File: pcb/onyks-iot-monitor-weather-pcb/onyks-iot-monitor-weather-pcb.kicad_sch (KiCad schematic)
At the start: 17 parts, among them SW1 BOOT, SW2 ENABLE, U1 ESP32-WROOM-32D, U2 SHT30-DIS

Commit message: Added schematic for our project
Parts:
- removed C6: C, symbol Device:C
- removed R2, R3: 10k, symbol Device:R
- removed U2: SHT30-DIS, Sensor_Humidity:Sensirion_DFN-8-1EP_2.5x2.5mm_P0.5mm_EP1.1x1.7mm, symbol Sensor_Humidity:SHT30-DIS
- added U10, U11, U12, U13, U8, U9: DRV5033AJxLPG, Package_TO_SOT_THT:TO-92_Inline, symbol Sensor_Magnetic:DRV5033AJxLPG
- added U2, U7: AMS1117, Package_TO_SOT_SMD:SOT-223-3_TabPin2, symbol Regulator_Linear:AMS1117
- added U3: AM2302, Sensor:ASAIR_AM2302_P2.54mm_Vertical, symbol Sensor:AM2302
- added U4: ~, symbol 1BMoje:PMS5003
- added U5: ~, symbol 1BMoje:SEN0219
- added U6: BMP280, Package_LGA:Bosch_LGA-8_2x2.5mm_P0.65mm_ClockwisePinNumbering, symbol Sensor_Pressure:BMP280
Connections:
- net GND: now also U1.1 (GND), U1.15 (GND), U1.38 (GND), U1.39 (GND), U10.2 (GND), U11.2 (GND), U12.2 (GND), U13.2 (GND), U2.1 (ADJ), U3.3 (GND), U3.4 (GND), U4.2 (GND), U5.3 (GND), U6.1 (GND), U6.7 (GND), U7.1 (ADJ), U8.2 (GND), U9.2 (GND)
- net VCC: now also U10.1 (VCC), U11.1 (VCC), U12.1 (VCC), U13.1 (VCC), U2.3 (VI), U3.1 (VDD), U4.1 (VCC), U5.2 (VCC), U7.3 (VI), U8.1 (VCC), U9.1 (VCC); no longer U1.2 (VDD)
- net Hall 1: now reaches U1.10 (IO25)
- net Hall 1: now also U9.3 (OUT)
- net Hall 2: now reaches U1.11 (IO26)
- net Hall 2: now also U8.3 (OUT)
- net Hall 3: now reaches U1.12 (IO27)
- net Hall 3: now also U10.3 (OUT)
- net Hall 6: now reaches U1.13 (IO14)
- net Hall 6: now also U12.3 (OUT)
- net BMP_SCK: now reaches U1.20 (SCK/CLK)
- net BMP_SCK: now also U6.4 (SCK)
- net BMP_SDO: now reaches U1.21 (SDO/SD0)
- net BMP_SDO: now also U6.5 (SDO)
- net BMP_SDI: now reaches U1.22 (SDI/SD1)
- net BMP_SDI: now also U6.3 (SDI)
- net PMS_SELECT: now reaches U1.23 (IO15)
- net PMS_SELECT: now also U4.8 (ModeSelect)
- net PMS_SET: now reaches U1.24 (IO2)
- net PMS_SET: now also U4.3 (SET)
- net PMS_RXD: now reaches U1.34 (RXD0/IO3)
- net PMS_RXD: now also U4.4 (RXD)
- net PMS_TXD: now reaches U1.35 (TXD0/IO1)
- net PMS_TXD: now also U4.5 (TXD)
- net PMS_RESET: now reaches U1.36 (IO22)
- net PMS_RESET: now also U4.6 (RESET)
- net Hall 5: now reaches U1.6 (IO34)
- net Hall 5: now also U13.3 (OUT)
- net PMS_PWM: now reaches U1.7 (IO35)
- net PMS_PWM: now also U4.7 (PWM)
- net Hall 4: now reaches U1.8 (IO32)
- net Hall 4: now also U11.3 (OUT)
- net SCL renamed SEN0219
- net SEN0219: now also U5.1 (Signal)
- net SDA renamed DHT22
- net DHT22: now also U3.2 (SDA)
- new net: U1.2 (VDD), U2.2 (VO)
- new net BMP_CSB: U6.2 (CSB), U6.6 (VDDIO), U6.8 (VDD), U7.2 (VO)
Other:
- note added: "BMP280 - pressure sensor"
- note added: "DHT22 - Temperature and humidity sensor"
- note added: "Hall effect sensors - quantity of rain"
- note added: "Hall effect sensors - wind direction"
- note added: "Hall effect sensors - wind speed"
- note added: "INFRARED CO2 sensor SEN0219"
- note added: "PMS5003 - Air quality sensor"
- note removed: "Temperature and Humidity Sensor"
- moved on the sheet: C1, C2, C3, C4, C5, D1, R1, R4, R5, R6, SW1, SW2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

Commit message: Updated schematics and added footprints and 3dmodels for the elements
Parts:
- removed D1: LED_KRGB, symbol Device:LED_KRGB
- removed R4, R5, R6: 300, symbol Device:R
- removed SW1: BOOT, symbol Switch:SW_Push
- removed SW2: ENABLE, symbol Switch:SW_Push
- removed U10, U11, U12, U13, U8, U9: DRV5033AJxLPG, Package_TO_SOT_THT:TO-92_Inline, symbol Sensor_Magnetic:DRV5033AJxLPG
- removed U3: AM2302, Sensor:ASAIR_AM2302_P2.54mm_Vertical, symbol Sensor:AM2302
- removed U4: ~, symbol 1BMoje:PMS5003
- removed U5: ~, symbol 1BMoje:SEN0219
- removed U7: AMS1117, Package_TO_SOT_SMD:SOT-223-3_TabPin2, symbol Regulator_Linear:AMS1117
- added J1, J2, J4, J5, J6, J7, J8, J9: 53398-0371, 1bmoje:53398-0371, symbol 1BMoje:53398-0371
- added J10: Conn_01x02_Pin, Connector_Molex:Molex_SL_171971-0002_1x02_P2.54mm_Vertical, symbol Connector:Conn_01x02_Pin
- added J3: 53048-0810, 530480810, symbol 1BMoje:53048-0810
- added Q1, Q2: SS8050, Package_TO_SOT_SMD:SOT-23, symbol Transistor_BJT:SS8050
- added R2, R3: 10K, Resistor_SMD:R_0201_0603Metric, symbol Device:R
- added S1: BOOT, 18259106, symbol 1BMoje:1825910-6
- added S2: ENABLE, 18259106, symbol 1BMoje:1825910-6
- C1: value 22 uF -> 22uF; footprint (none) -> Capacitor_SMD:C_0201_0603Metric
- C2: footprint (none) -> Capacitor_SMD:C_0201_0603Metric
- C3: value C -> 0.1uF; footprint (none) -> Capacitor_SMD:C_0201_0603Metric
- C4, C5: value 0.1 uF -> 0.1uF; footprint (none) -> Capacitor_SMD:C_0201_0603Metric
- R1: value R -> 10K; footprint (none) -> Resistor_SMD:R_0201_0603Metric
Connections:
- net BMP_CSB is gone; now on net 3V3: U6.2 (CSB), U6.6 (VDDIO), U6.8 (VDD)
- net DHT22: now also J9.2
- net EN: now also Q1.3 (C), S2.2 (COM_2), S2.4 (NO_2)
- net GND: now also J1.2, J2.2, J3.2, J4.2, J5.2, J6.2, J7.2, J8.3, J9.3, S1.1 (COM_1), S1.3 (NO_1), S2.1 (COM_1), S2.3 (NO_1)
- net Hall 1: now also J4.3
- net Hall 2: now also J5.3
- net Hall 3: now also J6.3
- net Hall 4: now also J7.3
- net Hall 5: now also J2.3
- net Hall 6: now also J1.3
- net IO0: now also Q2.2 (E), S1.2 (COM_2), S1.4 (NO_2)
- net PMS_PWM: now also J3.7
- net PMS_RESET: now also J3.6
- net PMS_RXD: now also J3.4
- net PMS_SELECT: now also J3.8
- net PMS_SET: now also J3.3
- net PMS_TXD: now also J3.5
- net SEN0219: now also J8.1
- net VCC: now also J1.1, J2.1, J3.1, J4.1, J5.1, J6.1, J7.1, J8.2, J9.1
- net 3V3: now reaches U1.2 (VDD), U2.2 (VO)
- new net: J10.1 (Pin_1), Q2.3 (C), R2.1
- new net: Q1.1 (B), R2.2
- new net: J10.2 (Pin_2), Q1.2 (E), R3.1
- new net: Q2.1 (B), R3.2
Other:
- note added: "For programming"

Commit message: Added PCBv1.0
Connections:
- net 3V3: now also C1.1, C2.1, R1.1
- net IO0: now also U1.25 (IO0)
- net VCC: no longer C1.1, C2.1, R1.1
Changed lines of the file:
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@@
 	(wire
 		(pts
+			(xy 260.35 45.72) (xy 265.43 45.72)
+		)
+		(stroke
+			(width 0)
+			(type default)
+		)
+	)
+	(wire
+		(pts
 			(xy 245.11 27.94) (xy 245.11 40.64)
 		)
@@
 		)
 	)
+	(label "IO0"
+		(at 265.43 45.72 0)
+		(fields_autoplaced yes)
+		(effects
+			(font
+				(size 1.27 1.27)
+			)
+			(justify left bottom)
+		)
+	)
 	(label "PMS_TXD"
 		(at 144.78 91.44 0)
@@
 		)
 	)
+	(label "3V3"
+		(at 187.96 35.56 0)
+		(fields_autoplaced yes)
+		(effects
+			(font
+				(size 1.27 1.27)
+			)
+			(justify left bottom)
+		)
+	)
 	(label "BMP_CSB"
 		(at 129.54 163.83 0)
@@
 		)
 	)
+	(label "3V3"
+		(at 187.96 82.55 0)
+		(fields_autoplaced yes)
+		(effects
+			(font
+				(size 1.27 1.27)
+			)
+			(justify left bottom)
+		)
+	)
 	(label "BMP_SDO"
 		(at 129.54 161.29 0)
@@
 	)
 	(symbol
-		(lib_id "power:VCC")
-		(at 187.96 82.55 0)
-		(unit 1)
-		(exclude_from_sim no)
-		(in_bom yes)
-		(on_board yes)
-		(dnp no)
-		(fields_autoplaced yes)
-		(property "Reference" "#PWR05"
-			(at 187.96 86.36 0)
-			(effects
-				(font
-					(size 1.27 1.27)
-				)
-				(hide yes)
-			)
-		)
-		(property "Value" "VCC"
-			(at 187.96 77.47 0)
-			(effects
-				(font
-					(size 1.27 1.27)
-				)
-			)
-		)
-		(property "Footprint" ""
-			(at 187.96 82.55 0)
-			(effects
-				(font
-					(size 1.27 1.27)
-				)
-				(hide yes)
-			)
-		)
-		(property "Datasheet" ""
-			(at 187.96 82.55 0)
-			(effects
-				(font
-					(size 1.27 1.27)
-				)
-				(hide yes)
-			)
-		)
-		(property "Description" "Power symbol creates a global label with name \"VCC\""
-			(at 187.96 82.55 0)
-			(effects
-				(font
-					(size 1.27 1.27)
-				)
-				(hide yes)
-			)
-		)
-		(pin "1"
-		)
-		(instances
-			(project "onyks-iot-monitor-weather-pcb"
-				(path "/c76e8e74-1f9a-4d6f-ac1c-451a63f003ec"
-					(reference "#PWR05")
-					(unit 1)
-				)
-			)
-		)
-	)
-	(symbol
 		(lib_id "Device:C")
 		(at 208.28 58.42 0)
@@
 					(unit 1)
 				)
-			)
-		)
-	)
-	(symbol
-		(lib_id "power:VCC")
-		(at 187.96 35.56 0)
-		(unit 1)
-		(exclude_from_sim no)
-		(in_bom yes)
-		(on_board yes)
-		(dnp no)
-		(fields_autoplaced yes)
-		(property "Reference" "#PWR03"
-			(at 187.96 39.37 0)
-			(effects
-				(font
-					(size 1.27 1.27)
-				)
-				(hide yes)
-			)
-		)
-		(property "Value" "VCC"
-			(at 187.96 30.48 0)
-			(effects
-				(font
-					(size 1.27 1.27)
-				)
-			)
-		)
-		(property "Footprint" ""
-			(at 187.96 35.56 0)
-			(effects
-				(font
-					(size 1.27 1.27)
-				)
-				(hide yes)
-			)
-		)
-		(property "Datasheet" ""
-			(at 187.96 35.56 0)
-			(effects
-				(font
-					(size 1.27 1.27)
-				)
-				(hide yes)
-			)
-		)
-		(property "Description" "Power symbol creates a global label with name \"VCC\""
-			(at 187.96 35.56 0)
-			(effects
-				(font
-					(size 1.27 1.27)
-				)
-				(hide yes)
-			)
-		)
-		(pin "1"
-		)
-		(instances
-			(project ""
-				(path "/c76e8e74-1f9a-4d6f-ac1c-451a63f003ec"
-					(reference "#PWR03")
-					(unit 1)
-				)

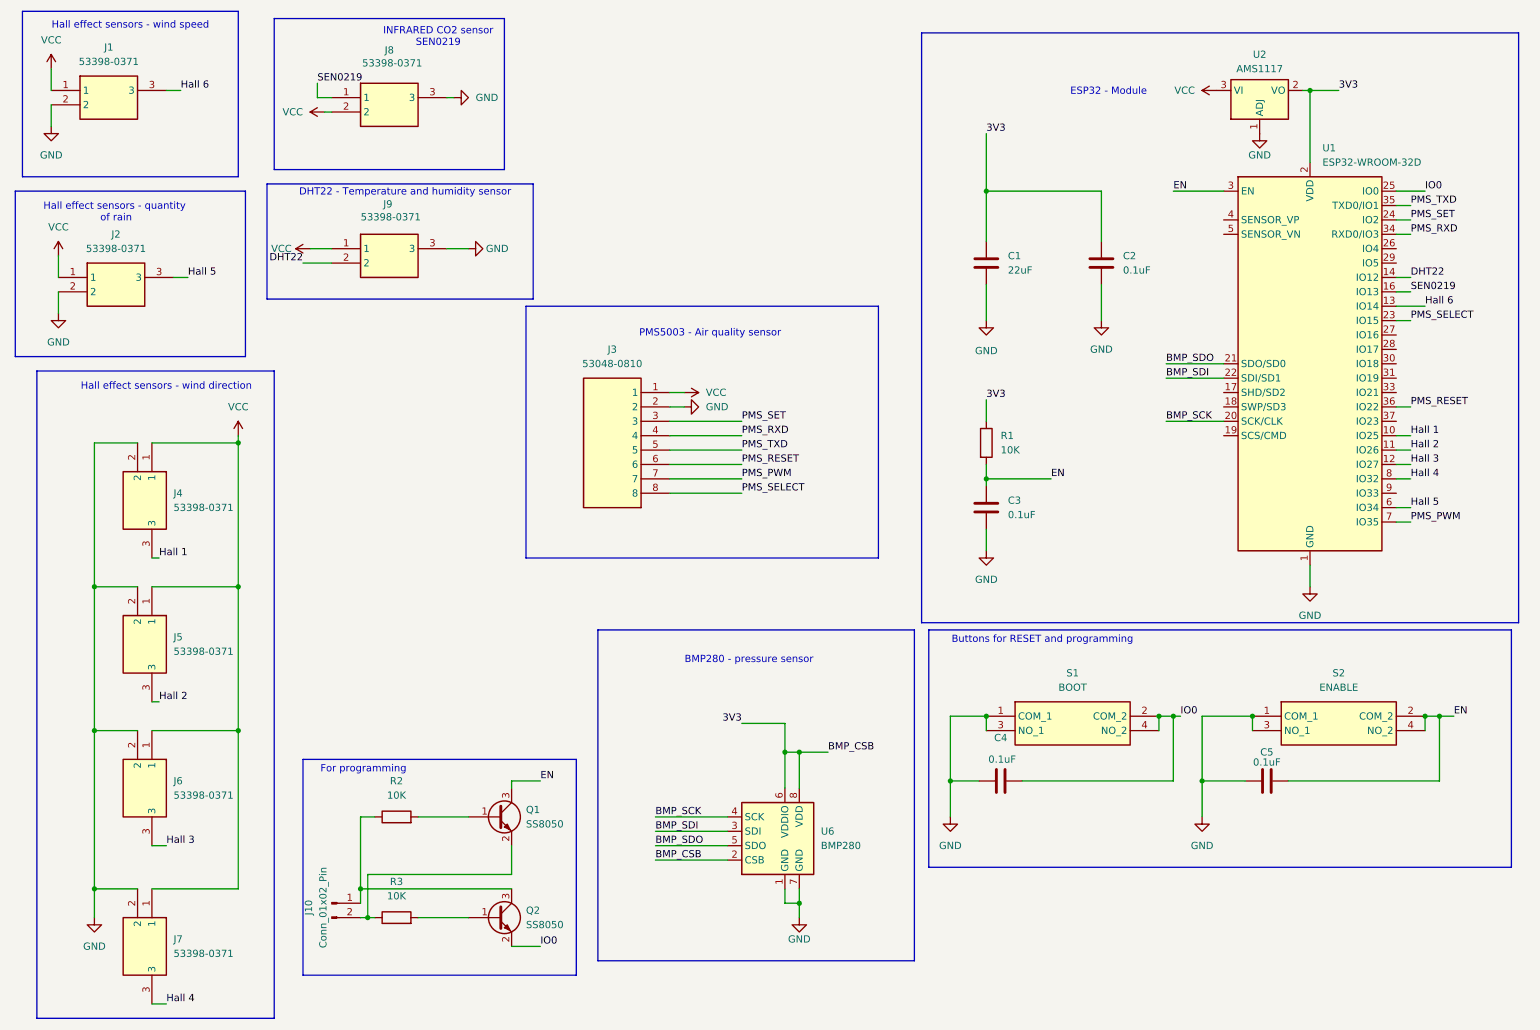
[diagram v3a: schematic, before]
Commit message: Updated schematic, changed and added couple of elements: 1.Changed buttons; 2.Changed Voltage Regulator; 3.Changed LED; 4.Added JTAG interface; 5.Added UART for programming; 6.Added other elements like capacitors etc.
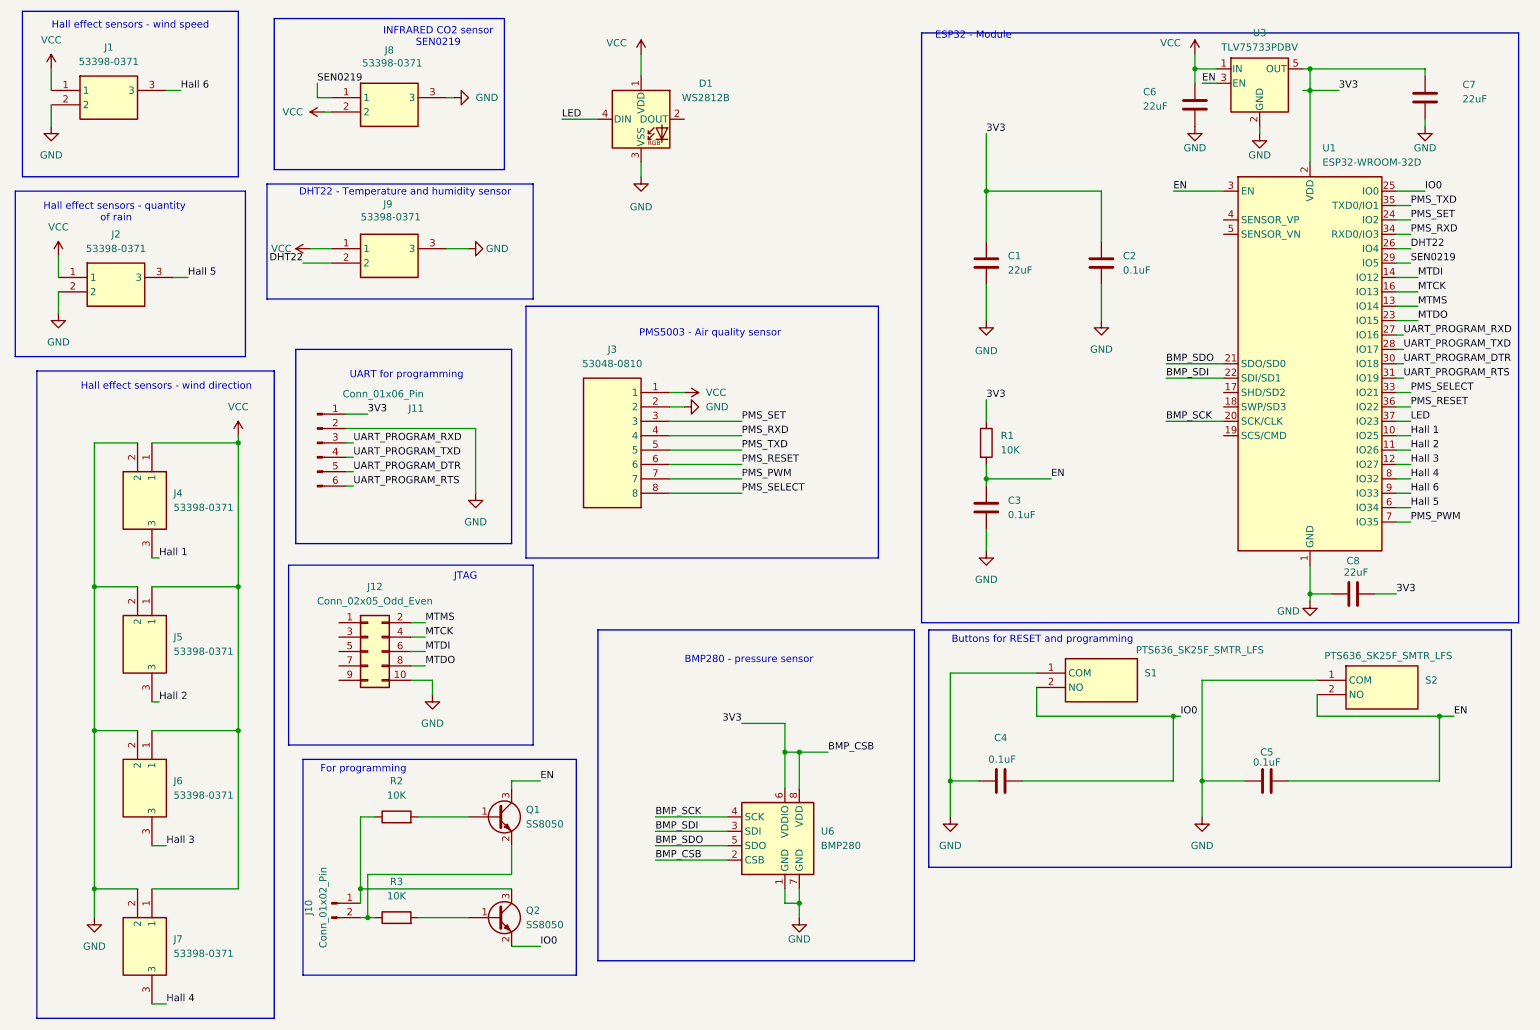
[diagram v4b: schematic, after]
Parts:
- removed S1: BOOT, 18259106, symbol 1BMoje:1825910-6
- removed S2: ENABLE, 18259106, symbol 1BMoje:1825910-6
- removed U2: AMS1117, Package_TO_SOT_SMD:SOT-223-3_TabPin2, symbol Regulator_Linear:AMS1117
- added C6, C7, C8: 22uF, Capacitor_SMD:C_0201_0603Metric, symbol Device:C
- added D1: WS2812B, LED_SMD:LED_WS2812B_PLCC4_5.0x5.0mm_P3.2mm, symbol LED:WS2812B
- added J11: Conn_01x06_Pin, Connector_PinHeader_2.54mm:PinHeader_1x06_P2.54mm_Vertical, symbol Connector:Conn_01x06_Pin
- added J12: Conn_02x05_Odd_Even, Connector_PinHeader_2.54mm:PinHeader_2x05_P2.54mm_Vertical, symbol Connector_Generic:Conn_02x05_Odd_Even
- added S1, S2: PTS636_SK25F_SMTR_LFS, 1bmoje:PTS636SK25FSMTRLFS, symbol 1BMoje:PTS636_SK25F_SMTR_LFS
- added U3: TLV75733PDBV, Package_TO_SOT_SMD:SOT-23-5, symbol Regulator_Linear:TLV75733PDBV
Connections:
- net 3V3: now also C7.1, C8.2, J11.1 (Pin_1), U3.5 (OUT)
- net DHT22: now also U1.26 (IO4); no longer U1.14 (IO12)
- net EN: now also S2.2 (NO), U3.3 (EN)
- net GND: now also C6.2, C7.2, C8.1, D1.3 (VSS), J11.2 (Pin_2), J12.10 (Pin_10), S1.1 (COM), S2.1 (COM), U3.2 (GND)
- net Hall 6: now also U1.9 (IO33); no longer U1.13 (IO14)
- net IO0: now also S1.2 (NO)
- net PMS_SELECT: now also U1.33 (IO21); no longer U1.23 (IO15)
- net SEN0219: now also U1.29 (IO5); no longer U1.16 (IO13)
- net VCC: now also C6.1, D1.1 (VDD), U3.1 (IN)
- net UART_PROGRAM_RXD: now reaches U1.27 (IO16)
- net UART_PROGRAM_RXD: now also J11.3 (Pin_3)
- net UART_PROGRAM_TXD: now reaches U1.28 (IO17)
- net UART_PROGRAM_TXD: now also J11.4 (Pin_4)
- net UART_PROGRAM_DTR: now reaches U1.30 (IO18)
- net UART_PROGRAM_DTR: now also J11.5 (Pin_5)
- net UART_PROGRAM_RTS: now reaches U1.31 (IO19)
- net UART_PROGRAM_RTS: now also J11.6 (Pin_6)
- net LED: now reaches U1.37 (IO23)
- net LED: now also D1.4 (DIN)
- new net MTCK: J12.4 (Pin_4), U1.16 (IO13)
- new net MTDI: J12.6 (Pin_6), U1.14 (IO12)
- new net MTDO: J12.8 (Pin_8), U1.23 (IO15)
- new net MTMS: J12.2 (Pin_2), U1.13 (IO14)
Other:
- note added: "JTAG"
- note added: "UART for programming"

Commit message: Done my version of PCB
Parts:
- added J13: Conn_01x02_Pin, Connector_PinHeader_2.54mm:PinHeader_1x02_P2.54mm_Vertical, symbol Connector:Conn_01x02_Pin
- J10: footprint Connector_Molex:Molex_SL_171971-0002_1x02_P2.54mm_Vertical -> Connector_PinHeader_2.54mm:PinHeader_1x02_P2.54mm_Vertical
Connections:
- net 3V3: now also J12.1 (Pin_1)
- net GND: now also J12.3 (Pin_3), J12.5 (Pin_5), J12.9 (Pin_9), J13.2 (Pin_2)
- net MTDI: now also J12.8 (Pin_8); no longer J12.6 (Pin_6)
- net MTDO: now also J12.6 (Pin_6); no longer J12.8 (Pin_8)
- net VCC: now also J13.1 (Pin_1)
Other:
- note added: "Power Supply"

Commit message: CheckedJLCPCBDesignRules, the only remaining errors are due to holes in esp 32 module
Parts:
- C1, C2, C3, C4, C5, C6, C7, C8: footprint Capacitor_SMD:C_0201_0603Metric -> Capacitor_SMD:C_0603_1608Metric
- R1, R2, R3: footprint Resistor_SMD:R_0201_0603Metric -> Resistor_SMD:R_0603_1608Metric
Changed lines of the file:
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@@
 			)
 		)
-		(property "Footprint" "Capacitor_SMD:C_0201_0603Metric"
+		(property "Footprint" "Capacitor_SMD:C_0603_1608Metric"
 			(at 188.9252 105.41 0)
 			(effects
@@
 			)
 		)
-		(property "Footprint" "Capacitor_SMD:C_0201_0603Metric"
+		(property "Footprint" "Capacitor_SMD:C_0603_1608Metric"
 			(at 266.3952 33.02 0)
 			(effects
@@
 			)
 		)
-		(property "Footprint" "Capacitor_SMD:C_0201_0603Metric"
+		(property "Footprint" "Capacitor_SMD:C_0603_1608Metric"
 			(at 188.9252 62.23 0)
 			(effects
@@
 			)
 		)
-		(property "Footprint" "Resistor_SMD:R_0201_0603Metric"
+		(property "Footprint" "Resistor_SMD:R_0603_1608Metric"
 			(at 83.82 157.988 90)
 			(effects
@@
 			)
 		)
-		(property "Footprint" "Capacitor_SMD:C_0201_0603Metric"
+		(property "Footprint" "Capacitor_SMD:C_0603_1608Metric"
 			(at 209.2452 62.23 0)
 			(effects
@@
 			)
 		)
-		(property "Footprint" "Capacitor_SMD:C_0201_0603Metric"
+		(property "Footprint" "Capacitor_SMD:C_0603_1608Metric"
 			(at 194.31 148.8948 0)
 			(effects
@@
 			)
 		)
-		(property "Footprint" "Capacitor_SMD:C_0201_0603Metric"
+		(property "Footprint" "Capacitor_SMD:C_0603_1608Metric"
 			(at 225.7552 34.29 0)
 			(effects
@@
 			)
 		)
-		(property "Footprint" "Resistor_SMD:R_0201_0603Metric"
+		(property "Footprint" "Resistor_SMD:R_0603_1608Metric"
 			(at 83.82 175.768 90)
 			(effects
@@
 			)
 		)
-		(property "Footprint" "Resistor_SMD:R_0201_0603Metric"
+		(property "Footprint" "Resistor_SMD:R_0603_1608Metric"
 			(at 186.182 90.17 90)
 			(effects
@@
 			)
 		)
-		(property "Footprint" "Capacitor_SMD:C_0201_0603Metric"
+		(property "Footprint" "Capacitor_SMD:C_0603_1608Metric"
 			(at 256.54 115.8748 0)
 			(effects
@@
 			)
 		)
-		(property "Footprint" "Capacitor_SMD:C_0201_0603Metric"
+		(property "Footprint" "Capacitor_SMD:C_0603_1608Metric"
 			(at 241.3 148.8948 0)
 			(effects
